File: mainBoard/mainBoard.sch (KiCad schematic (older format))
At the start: 37 parts

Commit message: Main board and proto-board added
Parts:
- removed C? (x17): 100nF, w_smd_cap:c_0603, symbol C
- removed C?: 4.7µF, iwasz:c_tant_A-pins21, symbol C
- removed C?: 1µF, w_smd_cap:c_0603, symbol C
- removed C? (x2): 10pF, w_smd_cap:c_0603, symbol C
- removed C?: 4.7µF, iwasz:c_tant_A-pins21, symbol CP
- removed C? (x2): 6pF, w_smd_cap:c_0603, symbol C
- removed D?: LED, symbol Device:LED
- removed P?: pgm, iwasz:00-9159-8PIN, symbol CONN_8
- removed P? (x2): CONN_1, Measurement_Points:Measurement_Point_Round-SMD-Pad_Small, symbol CONN_1
- removed R?: 220R, w_smd_resistors:r_0402, symbol R
- removed R?: 680R, w_smd_resistors:r_0402, symbol R
- removed R? (x2): 22R, w_smd_resistors:r_0402, symbol R
- removed R?: 70k, w_smd_resistors:r_0402, symbol R
- removed R?: 10k, w_smd_resistors:r_0402, symbol R
- removed U?: STM32F407VGTx, LQFP100, symbol MCU_ST_STM32:STM32F407VGTx
- removed Y?: 16MHz, Crystals_Oscillators_SMD:crystal_FA238-TSX3225, symbol Crystal
- removed Y?: 32kHz, iwasz:crystal_3.2_1.5, symbol Crystal
- added C1, C11, C14, C15, C16, C17, C18, C19, C2, C21, C22, C3, C4, C5, C6, C7, C8: 100nF, Capacitor_SMD:C_0603_1608Metric, symbol Device:C
- added C10, C12, C13, C9: 10pF, Capacitor_SMD:C_0603_1608Metric, symbol Device:C
- added C20: 4.7µF, Capacitor_SMD:C_1206_3216Metric, symbol Device:C
- added C23, C24: 2.2µF, Capacitor_SMD:C_1206_3216Metric, symbol Device:C
- added C25, C26: 1µF, Capacitor_SMD:C_0805_2012Metric, symbol Device:C
- added D1: LED, LED_SMD:LED_0805_2012Metric, symbol Device:LED
- added D2: BAT60JFILM, Diode_SMD:D_SOD-323, symbol Device:D_Schottky
- added J1: program, Connector_PinHeader_2.00mm:PinHeader_1x07_P2.00mm_Vertical, symbol Connector_Generic:Conn_01x07
- added J2: uniwersal-board2, iwasz:uniwersal-board, symbol iwasz-kicad:uniwersal-board2
- added JP1: led1, Jumper:SolderJumper-2_P1.3mm_Open_RoundedPad1.0x1.5mm, symbol Jumper:SolderJumper_2_Open
- added JP10: usbVbus, Jumper:SolderJumper-2_P1.3mm_Open_RoundedPad1.0x1.5mm, symbol Jumper:SolderJumper_2_Open
- added JP11, JP13: x, Jumper:SolderJumper-2_P1.3mm_Open_RoundedPad1.0x1.5mm, symbol Jumper:SolderJumper_2_Open
- added JP12: x32, Jumper:SolderJumper-2_P1.3mm_Bridged_RoundedPad1.0x1.5mm, symbol Jumper:SolderJumper_2_Open
- added JP2: boot0, Jumper:SolderJumper-2_P1.3mm_Open_RoundedPad1.0x1.5mm, symbol Jumper:SolderJumper_2_Open
- added JP3, JP5: boot1, Jumper:SolderJumper-2_P1.3mm_Open_RoundedPad1.0x1.5mm, symbol Jumper:SolderJumper_2_Open
- added JP4: consoleTx, Jumper:SolderJumper-2_P1.3mm_Bridged_RoundedPad1.0x1.5mm, symbol Jumper:SolderJumper_2_Open
- added JP6: consoleRx, Jumper:SolderJumper-2_P1.3mm_Bridged_RoundedPad1.0x1.5mm, symbol Jumper:SolderJumper_2_Open
- added JP7: usbDp, Jumper:SolderJumper-2_P1.3mm_Bridged_RoundedPad1.0x1.5mm, symbol Jumper:SolderJumper_2_Open
- added JP8: usbDm, Jumper:SolderJumper-2_P1.3mm_Bridged_RoundedPad1.0x1.5mm, symbol Jumper:SolderJumper_2_Open
- added JP9: usbId, Jumper:SolderJumper-2_P1.3mm_Open_RoundedPad1.0x1.5mm, symbol Jumper:SolderJumper_2_Open
- added R1: 220, Resistor_SMD:R_0603_1608Metric, symbol Device:R
- added R10, R7, R8, R9: 22, Resistor_SMD:R_0603_1608Metric, symbol Device:R
- added R2: 680, Resistor_SMD:R_0603_1608Metric, symbol Device:R
- added R3: 10k, Resistor_SMD:R_0603_1608Metric, symbol Device:R
- added R4, R5, R6: 510, Resistor_SMD:R_0603_1608Metric, symbol Device:R
- added SW1: reset, Button_Switch_THT:SW_Tactile_SPST_Angled_PTS645Vx83-2LFS, symbol Switch:SW_Push
- added U1: STM32F407VGTx, Package_QFP:LQFP-100_14x14mm_P0.5mm, symbol iwasz-kicad:STM32F407VGTx
- added U2: SMF05C / MMQA5V6T3G, Package_TO_SOT_SMD:SOT-363_SC-70-6, symbol iwasz-kicad:SMF05C
- added U3: usb-micro, iwasz:conn_usb_B_micro_smd-2-nohole, symbol iwasz-kicad:usb-micro
- added U4: MIC5504-3.3YM5, Package_TO_SOT_SMD:SOT-23-5, symbol Regulator_Linear:MIC5504-3.3YM5
- added Y1: 32kHz, Crystal:Crystal_C38-LF_D3.0mm_L8.0mm_Horizontal, symbol Device:Crystal
- added Y2: 8/16MHz, Crystal:Crystal_HC49-4H_Vertical, symbol Device:Crystal
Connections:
- net labels added: +12V, +5V, nrst, pa0, pa1, pa10, pa11, pa12, pa15, pa2, pa3, pa4, pa5, pa6, pa7, pa8, pa9, pb0, pb1, pb10, pb11, pb12, pb13, pb14, pb15, pb2, pb3, pb4, pb5, pb6, pb7, pb8, pb9, pc0, pc1, pc10, pc11, pc12, pc13, pc14, pc15, pc2, pc3, pc4, pc5, pc6, pc7, pc8, pc9, pd0, pd1, pd10, pd11, pd12, pd13, pd14, pd15, pd2, pd3, pd4, pd5, pd6, pd7, pd8, pd9, pe0, pe1, pe10, pe11, pe12, pe13, pe14, pe15, pe2, pe3, pe4, pe5, pe6, pe7, pe8, pe9, ph0, ph1
- net labels removed: VDD, gps_reset, gps_rx, gps_tx, gsm_pwrkey, gsm_rf_sync, gsm_rxd, gsm_status, gsm_txd, obd_canrx, obd_cantx, obd_io, obd_krx, obd_ktx, vSense
- wire segments 122 -> 182
- no-connect marks 29 -> 1
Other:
- note added: "10V"
- note added: "consoleRx should be connected to terminal's RX"
- note added: "consoleTx should be connected to terminal's TX"
- note removed: "*"
- note removed: "Blisko VDD i VSS, może pod spodem?"
- note removed: "Dać takie same headery jak w izzyDrive,\nWyprowadzić też reset do tego headeru."
- note removed: "Uwaga, tu dać może MLCC,\ntylko sprawdzić jaka wielkość\nobudowy."
- note removed: "Uwaga, znów pomyliłem, przelutwoać na 8.4\nW schemacie (tutaj) już poprawione"
- note removed: "reset\n"

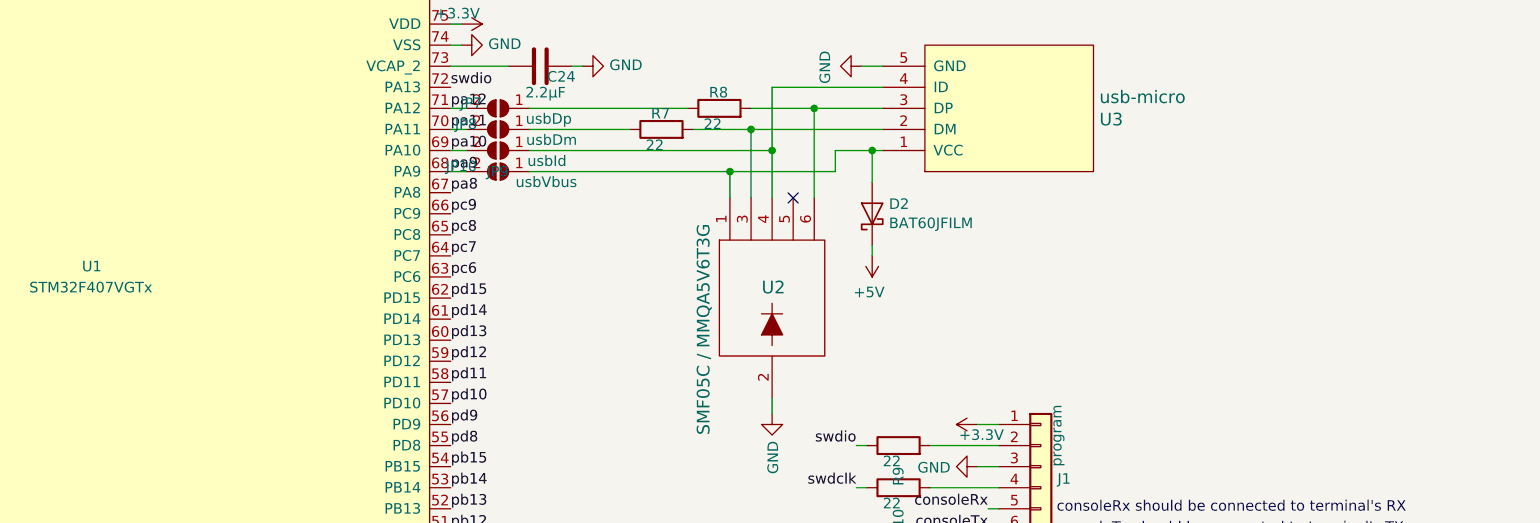
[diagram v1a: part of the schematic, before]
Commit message: Gerbers directory added, and domcumentation improved
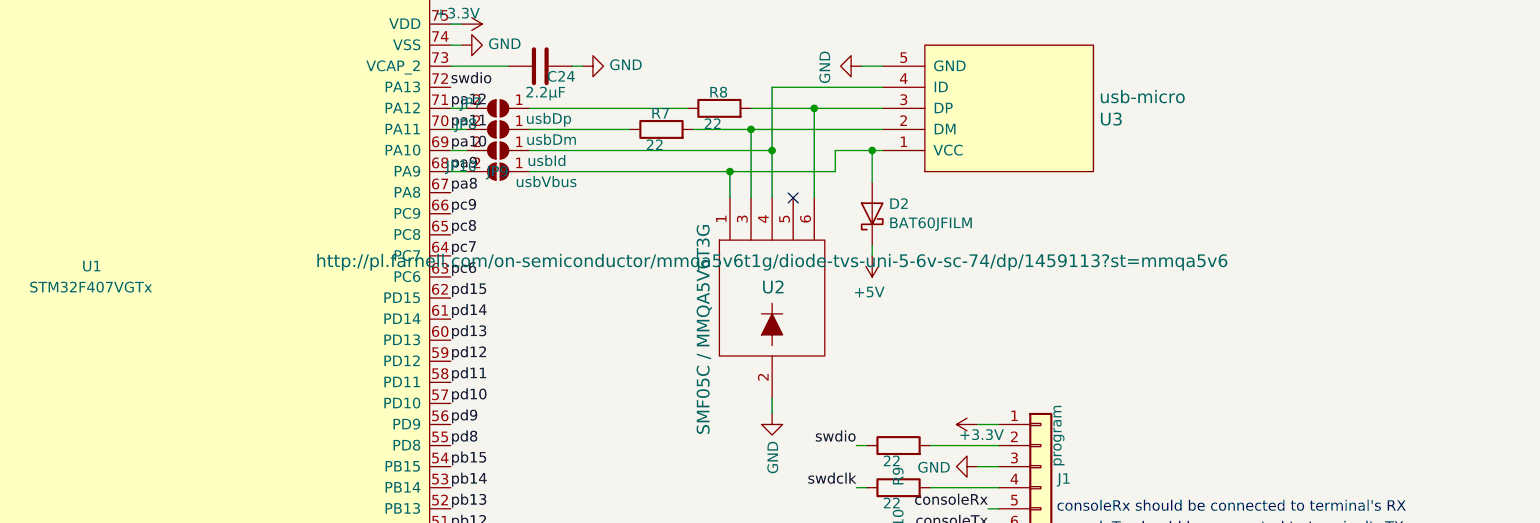
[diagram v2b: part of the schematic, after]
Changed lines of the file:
@@
 F 1 "STM32F407VGTx" H 5925 3900 50  0000 L CNN
 F 2 "Package_QFP:LQFP-100_14x14mm_P0.5mm" H 6225 3950 50  0001 C CNN
-F 3 "" H 6225 3950 50  0001 C CNN
+F 3 "http://pl.farnell.com/stmicroelectronics/stm32f407vgt6/mcu-32bit-cortex-m4-168mhz-lqfp/dp/2064368?st=stm32f407vgt" H 6225 3950 50  0001 C CNN
 	1    6225 3950
 	1    0    0    -1
@@
 F 1 "SMF05C / MMQA5V6T3G" V 9125 3050 60  0000 L CNN
 F 2 "Package_TO_SOT_SMD:SOT-363_SC-70-6" H 9450 3875 60  0001 C CNN
-F 3 "" H 9450 3875 60  0000 C CNN
+F 3 "http://pl.farnell.com/on-semiconductor/mmqa5v6t1g/diode-tvs-uni-5-6v-sc-74/dp/1459113?st=mmqa5v6" H 9450 3875 60  0000 C CNN
 	1    9450 3875
 	1    0    0    -1
@@
 F 1 "BAT60JFILM" V 9880 3571 50  0000 R CNN
 F 2 "Diode_SMD:D_SOD-323" H 9925 3650 50  0001 C CNN
-F 3 "" H 9925 3650 50  0001 C CNN
+F 3 "http://pl.farnell.com/stmicroelectronics/bat60jfilm/diode-schottky-3a-10v-smd/dp/1467544?st=BAT60JFILM" H 9925 3650 50  0001 C CNN
 	1    9925 3650
 	0    -1   -1   0

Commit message: Bug-fixes. 3 battery soldered and working.
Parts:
- JP4: value consoleTx -> consoleRx
- JP6: value consoleRx -> consoleTx
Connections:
- net consoleRx: now also J1.6 (Pin_6), JP4.1 (A); no longer J1.5 (Pin_5), JP6.1 (A)
- net consoleTx: now also J1.5 (Pin_5), JP6.1 (A); no longer J1.6 (Pin_6), JP4.1 (A)
- net swdclk: now also R9.1; no longer R10.1
- net swdio: now also R10.1; no longer R9.1
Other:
- note added: "zły footprint"
- note removed: "consoleRx should be connected to terminal's RX"
- note removed: "consoleTx should be connected to terminal's TX"
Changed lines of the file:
@@
 Wire Wire Line
 	10425 5250 10525 5250
+Text Label 9850 4950 2    50   ~ 0
+swdio
 Text Label 9850 4750 2    50   ~ 0
-swdio
-Text Label 9850 4950 2    50   ~ 0
 swdclk
+Text Label 10475 5150 2    50   ~ 0
+consoleRx
 Text Label 10475 5050 2    50   ~ 0
-consoleRx
-Text Label 10475 5150 2    50   ~ 0
 consoleTx
 Text Label 7925 3050 0    50   ~ 0
@@
 swdclk
 Text Label 6100 1475 1    50   ~ 0
-consoleTx
-Text Notes 10800 5075 0    50   ~ 0
-consoleRx should be connected to terminal's RX
-Text Notes 10800 5175 0    50   ~ 0
-consoleTx should be connected to terminal's TX
+consoleRx
 $Comp
 L iwasz-kicad:SMF05C U2
@@
 F 1 "SMF05C / MMQA5V6T3G" V 9125 3050 60  0000 L CNN
 F 2 "Package_TO_SOT_SMD:SOT-363_SC-70-6" H 9450 3875 60  0001 C CNN
-F 3 "http://pl.farnell.com/on-semiconductor/mmqa5v6t1g/diode-tvs-uni-5-6v-sc-74/dp/1459113?st=mmqa5v6" H 9450 3875 60  0000 C CNN
+F 3 "http://pl.farnell.com/on-semiconductor/mmqa5v6t1g/diode-tvs-uni-5-6v-sc-74/dp/1459113?st=mmqa5v6" H 9450 3875 60  0001 C CNN
 	1    9450 3875
 	1    0    0    -1
@@
 P 6100 1625
 F 0 "JP4" V 6025 1500 50  0000 L CNN
-F 1 "consoleTx" H 6100 1675 50  0000 L CNN
+F 1 "consoleRx" H 6100 1675 50  0000 L CNN
 F 2 "Jumper:SolderJumper-2_P1.3mm_Bridged_RoundedPad1.0x1.5mm" H 6100 1625 50  0001 C CNN
 F 3 "~" H 6100 1625 50  0001 C CNN
@@
 	6100 2000 6100 1775
 Text Label 6275 1475 1    50   ~ 0
-consoleRx
+consoleTx
 $Comp
 L Jumper:SolderJumper_2_Open JP6
@@
 P 6275 1625
 F 0 "JP6" V 6200 1500 50  0000 L CNN
-F 1 "consoleRx" H 6275 1675 50  0000 L CNN
+F 1 "consoleTx" H 6275 1675 50  0000 L CNN
 F 2 "Jumper:SolderJumper-2_P1.3mm_Bridged_RoundedPad1.0x1.5mm" H 6275 1625 50  0001 C CNN
 F 3 "~" H 6275 1625 50  0001 C CNN
@@
 Wire Wire Line
 	1200 5475 1250 5475
+Text Notes 9500 4425 0    50   ~ 0
+zły footprint
 $EndSCHEMATC
